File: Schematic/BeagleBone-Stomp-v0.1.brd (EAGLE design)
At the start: 100 x 80 mm, 8 parts, among them U1 MSP430G2553_RHB_32, U2 TLV320AIC3120_RHB_32

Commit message: connected a few of the pins in the design.
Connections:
- removed net AVDD: U2.17
- removed net SPKVDD: U2.24
- removed net SPKVSS: U2.25
- new net N$1: U$2.52, U2.24
- net 3.3V: now also U2.17
- net AVSS: no longer U2.16
- net GND: now also U2.16, U2.25
- net VDD_5V: no longer U$2.52
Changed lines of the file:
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@@
 <signal name="VDD_5V">
 <contactref element="U$2" pad="51"/>
-<contactref element="U$2" pad="52"/>
-<wire x1="69.85" y1="61.595" x2="69.85" y2="64.135" width="0" layer="19" extent="1-1"/>
-</signal>
-<signal name="VDD_ADC">
-<contactref element="U$2" pad="78"/>
-</signal>
-<signal name="GNDA_ADC">
-<contactref element="U$2" pad="80"/>
 </signal>
 <signal name="AGND">
@@
 <contactref element="U$2" pad="50"/>
 <contactref element="U$2" pad="49"/>
+<contactref element="U2" pad="17"/>
 <wire x1="72.39" y1="61.595" x2="72.39" y2="64.135" width="0" layer="19" extent="1-1"/>
+<wire x1="45.0088" y1="45.2374" x2="72.39" y2="61.595" width="0" layer="19" extent="1-1"/>
 </signal>
 <signal name="GND">
@@
 <contactref element="U$2" pad="90"/>
 <contactref element="U$2" pad="48"/>
-<wire x1="21.59" y1="64.135" x2="19.05" y2="64.135" width="0" layer="19" extent="1-1"/>
-<wire x1="19.05" y1="61.595" x2="19.05" y2="64.135" width="0" layer="19" extent="1-1"/>
-<wire x1="21.59" y1="61.595" x2="21.59" y2="64.135" width="0" layer="19" extent="1-1"/>
-<wire x1="74.93" y1="64.135" x2="21.59" y2="64.135" width="0" layer="19" extent="1-1"/>
+<contactref element="U2" pad="16"/>
+<contactref element="U2" pad="25"/>
 <wire x1="74.93" y1="61.595" x2="74.93" y2="64.135" width="0" layer="19" extent="1-1"/>
-<wire x1="74.93" y1="15.875" x2="74.93" y2="61.595" width="0" layer="19" extent="1-1"/>
+<wire x1="44.2976" y1="49.4538" x2="74.93" y2="61.595" width="0" layer="19" extent="1-1"/>
+<wire x1="44.2976" y1="44.5262" x2="44.2976" y2="49.4538" width="0" layer="19" extent="1-1"/>
+<wire x1="21.59" y1="61.595" x2="44.2976" y2="49.4538" width="0" layer="19" extent="1-1"/>
+<wire x1="21.59" y1="64.135" x2="21.59" y2="61.595" width="0" layer="19" extent="1-1"/>
+<wire x1="19.05" y1="64.135" x2="21.59" y2="64.135" width="0" layer="19" extent="1-1"/>
+<wire x1="19.05" y1="61.595" x2="21.59" y2="61.595" width="0" layer="19" extent="1-1"/>
+<wire x1="74.93" y1="15.875" x2="44.2976" y2="44.5262" width="0" layer="19" extent="1-1"/>
 <wire x1="74.93" y1="13.335" x2="74.93" y2="15.875" width="0" layer="19" extent="1-1"/>
 </signal>
@@
 <signal name="AVSS">
 <contactref element="U1" pad="27"/>
-<contactref element="U2" pad="16"/>
-<wire x1="43.307" y1="38.6588" x2="44.2976" y2="44.5262" width="0" layer="19" extent="1-1"/>
 </signal>
 <signal name="DVSS">
@@
 <contactref element="U2" pad="3"/>
 </signal>
-<signal name="AVDD">
-<contactref element="U2" pad="17"/>
-</signal>
 <signal name="SPKVSS_2">
 <contactref element="U2" pad="20"/>
@@
 <signal name="SPKVDD_2">
 <contactref element="U2" pad="21"/>
-</signal>
-<signal name="SPKVDD">
-<contactref element="U2" pad="24"/>
-</signal>
-<signal name="SPKVSS">
-<contactref element="U2" pad="25"/>
 </signal>
 <signal name="HPVDD">
@@
 <contactref element="U2" pad="29"/>
 </signal>
+<signal name="VDD_ADC">
+<contactref element="U$2" pad="78"/>
+</signal>
+<signal name="GNDA_ADC">
+<contactref element="U$2" pad="80"/>
+</signal>
+<signal name="N$1">
+<contactref element="U2" pad="24"/>
+<contactref element="U$2" pad="52"/>
+<wire x1="45.0088" y1="48.7426" x2="69.85" y2="61.595" width="0" layer="19" extent="1-1"/>
+</signal>
 </signals>

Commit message: Making some changes
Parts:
- added C1, C3, C4: 0.1u, microbuilder:0402
- added FB1: (no value), microbuilder:_0402
- added R1: 28k, microbuilder:0402
- added R2: 56.2k, microbuilder:0402
- added U3: TPS73701_DRB_8, bone:DRB8_1P75X1P5
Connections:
- removed net DVCC: U1.30
- removed net DVDD: U2.3
- removed net DVSS: U1.28, U2.18
- removed net IOVDD: U2.2
- removed net IOVSS: U2.1
- new net 1.8V: C4.2, R1.1, U2.3, U3.1
- net 3.3V: now also C1.1, U1.30, U2.2, U3.5, U3.8
- net 5.0V: now also C3.1, U2.24
- net AGND: now also FB1.1, U2.16, U2.33
- net GND: now also C1.2, C3.2, FB1.2, R2.1, U1.28, U2.1, U2.18, U3.4, U3.9; no longer U2.16
- net N$1: now also C4.1, R1.2, R2.2, U3.3; no longer U$2.52, U2.24
- net VDD_5V: now also U$2.52
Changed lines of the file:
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@@
 <attribute name="PACKAGE_DESIGNATOR" value="RHB" x="42.545" y="46.99" size="1.778" layer="27" display="off"/>
 </element>
+<element name="C1" library="microbuilder" package="0402" value="0.1u" x="1.905" y="-1.27"/>
+<element name="C3" library="microbuilder" package="0402" value="0.1u" x="1.905" y="-6.35"/>
+<element name="U3" library="bone" package="DRB8_1P75X1P5" value="TPS73701_DRB_8" x="4.445" y="-10.795">
+<attribute name="DATASHEETURL" value="http://www.ti.com/lit/gpn/TPS73701" x="4.445" y="-10.795" size="1.778" layer="27" display="off"/>
+<attribute name="PIN_COUNT" value="8" x="4.445" y="-10.795" size="1.778" layer="27" display="off"/>
+<attribute name="GENERIC_PART_NUMBER" value="TPS73701" x="4.445" y="-10.795" size="1.778" layer="27" display="off"/>
+<attribute name="DESCRIPTION" value="Single Output LDO, 1A, Adj. (1.2 to 5.0V), Reverse Current Protection" x="4.445" y="-10.795" size="1.778" layer="27" display="off"/>
+<attribute name="FAMILY_NAME" value="SINGLE CHANNEL LDO" x="4.445" y="-10.795" size="1.778" layer="27" display="off"/>
+<attribute name="MANUFACTURER" value="Texas Instruments" x="4.445" y="-10.795" size="1.778" layer="27" display="off"/>
+<attribute name="INDUSTRY_STD_PKG_TYPE" value="SON" x="4.445" y="-10.795" size="1.778" layer="27" display="off"/>
+<attribute name="VENDOR" value="Texas Instruments" x="4.445" y="-10.795" size="1.778" layer="27" display="off"/>
+<attribute name="MANUFACTURER_PART_NUMBER" value="tps73701_drb_8" x="4.445" y="-10.795" size="1.778" layer="27" display="off"/>
+<attribute name="PACKAGE_DESIGNATOR" value="DRB" x="4.445" y="-10.795" size="1.778" layer="27" display="off"/>
+</element>
+<element name="R1" library="microbuilder" package="0402" value="28k" x="1.905" y="-13.97"/>
+<element name="R2" library="microbuilder" package="0402" value="56.2k" x="1.905" y="-16.51"/>
+<element name="C4" library="microbuilder" package="0402" value="0.1u" x="1.905" y="-19.05"/>
+<element name="FB1" library="microbuilder" package="_0402" value="" x="1.905" y="-22.225"/>
 </elements>
 <signals>
 <signal name="VDD_5V">
 <contactref element="U$2" pad="51"/>
+<contactref element="U$2" pad="52"/>
+<wire x1="69.85" y1="61.595" x2="69.85" y2="64.135" width="0" layer="19" extent="1-1"/>
 </signal>
 <signal name="AGND">
 <contactref element="U$2" pad="38"/>
+<contactref element="U2" pad="16"/>
+<contactref element="U2" pad="33"/>
+<contactref element="FB1" pad="1"/>
+<wire x1="42.545" y1="46.99" x2="44.2976" y2="44.5262" width="0" layer="19" extent="1-1"/>
+<wire x1="29.21" y1="13.335" x2="44.2976" y2="44.5262" width="0" layer="19" extent="1-1"/>
+<wire x1="1.397" y1="-22.225" x2="29.21" y2="13.335" width="0" layer="19" extent="1-1"/>
 </signal>
 <signal name="5.0V">
 <contactref element="U$2" pad="53"/>
 <contactref element="U$2" pad="54"/>
+<contactref element="U2" pad="24"/>
+<contactref element="C3" pad="1"/>
 <wire x1="67.31" y1="61.595" x2="67.31" y2="64.135" width="0" layer="19" extent="1-1"/>
+<wire x1="45.0088" y1="48.7426" x2="67.31" y2="61.595" width="0" layer="19" extent="1-1"/>
+<wire x1="1.255" y1="-6.35" x2="45.0088" y2="48.7426" width="0" layer="19" extent="1-1"/>
 </signal>
 <signal name="3.3V">
@@
 <contactref element="U$2" pad="49"/>
 <contactref element="U2" pad="17"/>
+<contactref element="U1" pad="30"/>
+<contactref element="C1" pad="1"/>
+<contactref element="U2" pad="2"/>
+<contactref element="U3" pad="8"/>
+<contactref element="U3" pad="5"/>
 <wire x1="72.39" y1="61.595" x2="72.39" y2="64.135" width="0" layer="19" extent="1-1"/>
 <wire x1="45.0088" y1="45.2374" x2="72.39" y2="61.595" width="0" layer="19" extent="1-1"/>
+<wire x1="40.0812" y1="48.2346" x2="45.0088" y2="45.2374" width="0" layer="19" extent="1-1"/>
+<wire x1="41.783" y1="38.6588" x2="45.0088" y2="45.2374" width="0" layer="19" extent="1-1"/>
+<wire x1="1.255" y1="-1.27" x2="41.783" y2="38.6588" width="0" layer="19" extent="1-1"/>
+<wire x1="5.9182" y1="-9.8298" x2="1.255" y2="-1.27" width="0" layer="19" extent="1-1"/>
+<wire x1="5.9182" y1="-11.7602" x2="5.9182" y2="-9.8298" width="0" layer="19" extent="1-1"/>
 </signal>
 <signal name="GND">
@@
 <contactref element="U$2" pad="90"/>
 <contactref element="U$2" pad="48"/>
-<contactref element="U2" pad="16"/>
+<contactref element="U1" pad="28"/>
 <contactref element="U2" pad="25"/>
+<contactref element="U2" pad="1"/>
+<contactref element="C3" pad="2"/>
+<contactref element="C1" pad="2"/>
+<contactref element="U3" pad="4"/>
+<contactref element="U3" pad="9"/>
+<contactref element="U3" pad="4"/>
+<contactref element="R2" pad="1"/>
+<contactref element="U2" pad="18"/>
+<contactref element="FB1" pad="2"/>
 <wire x1="74.93" y1="61.595" x2="74.93" y2="64.135" width="0" layer="19" extent="1-1"/>
 <wire x1="44.2976" y1="49.4538" x2="74.93" y2="61.595" width="0" layer="19" extent="1-1"/>
-<wire x1="44.2976" y1="44.5262" x2="44.2976" y2="49.4538" width="0" layer="19" extent="1-1"/>
-<wire x1="21.59" y1="61.595" x2="44.2976" y2="49.4538" width="0" layer="19" extent="1-1"/>
+<wire x1="45.0088" y1="45.7454" x2="44.2976" y2="49.4538" width="0" layer="19" extent="1-1"/>
+<wire x1="40.0812" y1="48.7426" x2="44.2976" y2="49.4538" width="0" layer="19" extent="1-1"/>
+<wire x1="42.799" y1="38.6588" x2="45.0088" y2="45.7454" width="0" layer="19" extent="1-1"/>
+<wire x1="21.59" y1="61.595" x2="40.0812" y2="48.7426" width="0" layer="19" extent="1-1"/>
 <wire x1="21.59" y1="64.135" x2="21.59" y2="61.595" width="0" layer="19" extent="1-1"/>
 <wire x1="19.05" y1="64.135" x2="21.59" y2="64.135" width="0" layer="19" extent="1-1"/>
 <wire x1="19.05" y1="61.595" x2="21.59" y2="61.595" width="0" layer="19" extent="1-1"/>
-<wire x1="74.93" y1="15.875" x2="44.2976" y2="44.5262" width="0" layer="19" extent="1-1"/>
+<wire x1="74.93" y1="15.875" x2="42.799" y2="38.6588" width="0" layer="19" extent="1-1"/>
 <wire x1="74.93" y1="13.335" x2="74.93" y2="15.875" width="0" layer="19" extent="1-1"/>
+<wire x1="2.555" y1="-1.27" x2="42.799" y2="38.6588" width="0" layer="19" extent="1-1"/>
+<wire x1="2.555" y1="-6.35" x2="2.555" y2="-1.27" width="0" layer="19" extent="1-1"/>
+<wire x1="4.445" y1="-10.795" x2="2.555" y2="-6.35" width="0" layer="19" extent="1-1"/>
+<wire x1="2.9718" y1="-11.7602" x2="4.445" y2="-10.795" width="0" layer="19" extent="1-1"/>
+<wire x1="1.255" y1="-16.51" x2="2.9718" y2="-11.7602" width="0" layer="19" extent="1-1"/>
+<wire x1="2.413" y1="-22.225" x2="1.255" y2="-16.51" width="0" layer="19" extent="1-1"/>
 </signal>
 <signal name="AVCC">
@@
 <signal name="AVSS">
 <contactref element="U1" pad="27"/>
-</signal>
-<signal name="DVSS">
-<contactref element="U1" pad="28"/>
-<contactref element="U2" pad="18"/>
-<wire x1="42.799" y1="38.6588" x2="45.0088" y2="45.7454" width="0" layer="19" extent="1-1"/>
-</signal>
-<signal name="DVCC">
-<contactref element="U1" pad="30"/>
-</signal>
-<signal name="IOVSS">
-<contactref element="U2" pad="1"/>
-</signal>
-<signal name="IOVDD">
-<contactref element="U2" pad="2"/>
-</signal>
-<signal name="DVDD">
-<contactref element="U2" pad="3"/>
 </signal>
 <signal name="SPKVSS_2">
@@
 <contactref element="U$2" pad="80"/>
 </signal>
+<signal name="1.8V">
+<contactref element="U2" pad="3"/>
+<contactref element="U3" pad="1"/>
+<contactref element="R1" pad="1"/>
+<contactref element="C4" pad="2"/>
+<wire x1="2.9718" y1="-9.8298" x2="40.0812" y2="47.752" width="0" layer="19" extent="1-1"/>
+<wire x1="1.255" y1="-13.97" x2="2.9718" y2="-9.8298" width="0" layer="19" extent="1-1"/>
+<wire x1="2.555" y1="-19.05" x2="1.255" y2="-13.97" width="0" layer="19" extent="1-1"/>
+</signal>
 <signal name="N$1">
-<contactref element="U2" pad="24"/>
-<contactref element="U$2" pad="52"/>
-<wire x1="45.0088" y1="48.7426" x2="69.85" y2="61.595" width="0" layer="19" extent="1-1"/>
+<contactref element="C4" pad="1"/>
+<contactref element="R1" pad="2"/>
+<contactref element="R2" pad="2"/>
+<contactref element="U3" pad="3"/>
+<wire x1="2.555" y1="-16.51" x2="1.255" y2="-19.05" width="0" layer="19" extent="1-1"/>
+<wire x1="2.555" y1="-13.97" x2="2.555" y2="-16.51" width="0" layer="19" extent="1-1"/>
+<wire x1="2.9718" y1="-11.1252" x2="2.555" y2="-13.97" width="0" layer="19" extent="1-1"/>
 </signal>
 </signals>

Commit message: Adding MSP430 connections
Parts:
- added C10, C11, C12, C2, C7, C9: 10u, microbuilder:0805
- added C13, C14, C5, C6, C8: 0.1u, microbuilder:0402
- added GND, RST, SPKM, SPKP, TST, VCC: WIREPAD2,15/1,0, wirepad:2,15/1,0
- added R10, R11, R12, R13, R14, R15, R16: 10k, microbuilder:0402
- added R3, R4, R5, R6, R7, R8, R9: 470, microbuilder:0402
- moved U3 75.9 mm to (40.6, 55.9)
- turned U1 to 90 degrees
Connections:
- removed net AVSS: U1.27
- removed net HPVDD: U2.28
- removed net HPVSS: U2.29
- new net N$10: C11.1, U2.14
- new net N$11: C12.1, U2.13
- new net N$12: JP2.6, U1.31
- new net N$13: JP2.14, R9.2
- new net N$14: JP2.15, R8.2
- new net N$15: JP2.16, R7.2
- new net N$16: JP2.17, R6.2
- new net N$17: JP2.1, U1.5
- new net N$18: JP2.2, U1.4
- new net N$19: JP2.4, U1.2
- new net N$20: JP2.5, U1.1
- new net N$21: JP2.3, U1.3
- new net N$22: JP2.18, R5.2
- new net N$23: JP2.19, R4.2
- new net N$24: JP2.20, R3.2
- new net N$25: JP1.19, U1.15
- new net N$26: JP1.20, U1.14
- new net N$27: JP1.14, U1.20
- new net N$28: JP1.15, U1.19
- new net N$29: JP1.16, U1.18
- new net N$3: SPKM.1, U2.23
- new net N$30: JP1.17, U1.17
- new net N$31: JP1.18, U1.16
- new net N$32: TST.1, U1.24
- new net N$33: RST.1, U1.23
- new net N$34: JP2.7, R16.2, U1.6
- new net N$35: JP2.8, R15.2, U1.7
- new net N$36: JP2.9, R14.2, U1.9
- new net N$37: JP2.10, R13.2, U1.10
- new net N$38: JP2.11, R12.2, U1.11
- new net N$39: JP2.12, R11.2, U1.12
- new net N$4: SPKP.1, U2.26
- new net N$40: JP2.13, R10.2, U1.13
- new net N$5: C10.1, U2.27
- new net N$6: C10.2, U$7.T
- new net N$7: C9.2, U$7.S
- new net N$8: C12.2, U$1.S
- new net N$9: C11.2, U$1.T
- net 1.8V: now also C5.1
- net 3.3V: now also C13.1, C14.1, C2.1, C6.1, C7.1, C8.1, JP3.1, JP3.2, JP3.3, JP3.4, JP3.5, JP3.6, R10.1, R11.1, R12.1, R13.1, R14.1, R15.1, R16.1, R3.1, R4.1, R5.1, R6.1, R7.1, R8.1, R9.1, U1.29, U2.28, VCC.1
- net AGND: now also C13.2, C2.2, C6.2, U1.27, U1.33
- net AVCC: no longer U1.29
- net GND: now also C14.2, C5.2, C7.2, C8.2, C9.1, GND.1, JP1.1, JP1.10, JP1.11, JP1.12, JP1.13, JP1.2, JP1.3, JP1.4, JP1.5, JP1.6, JP1.7, JP1.8, JP1.9, U2.29

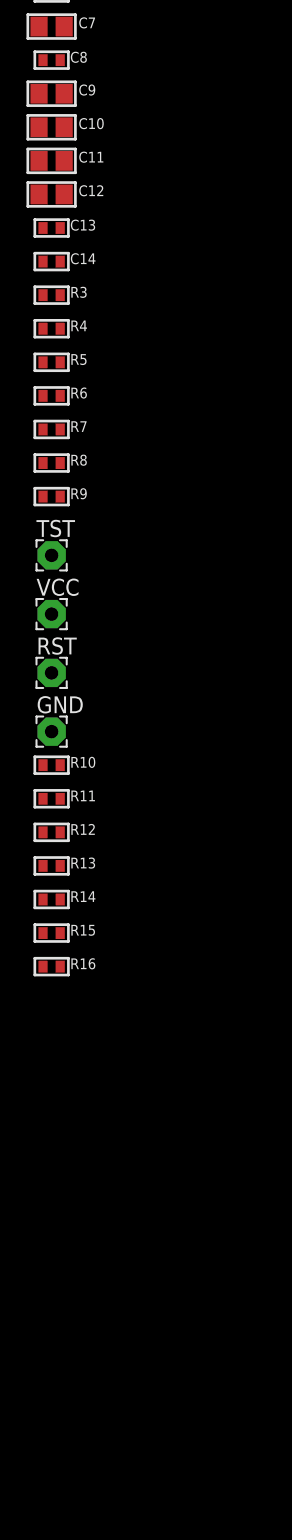
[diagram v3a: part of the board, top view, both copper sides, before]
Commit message: Adding crystal and a couple caps. Also added codec connections
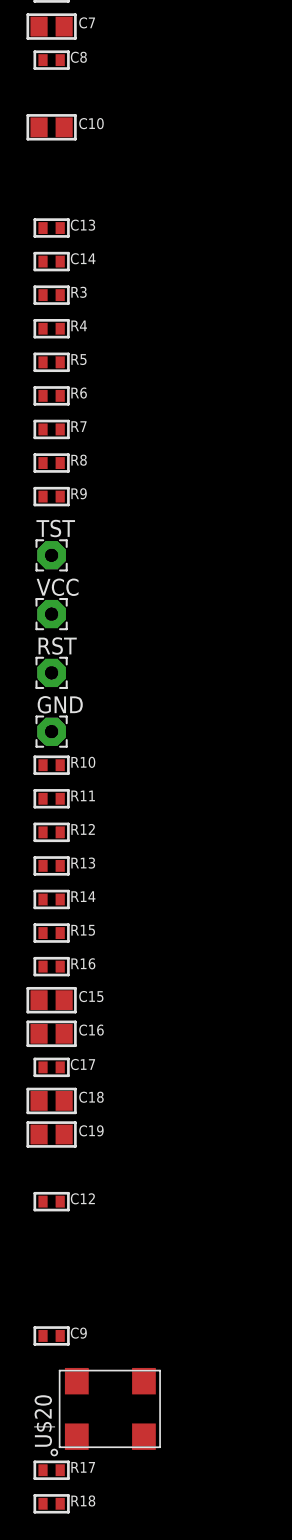
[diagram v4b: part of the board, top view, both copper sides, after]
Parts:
- removed C11: 10u, microbuilder:0805
- added C15, C16: 22u, microbuilder:0805
- added C17: 0.1u, microbuilder:0402
- added C18, C19: 10u, microbuilder:0805
- added R17, R18: 4.7k, microbuilder:0402
- added U$20: FXO-HC735-12, bone:FXO-HC735-12
- C10: value 10u -> 47u
- C12: value 10u -> 0.1u; device microbuilder:0805 -> microbuilder:0402
- C9: value 10u -> 0.01u; device microbuilder:0805 -> microbuilder:0402
- moved C9 94.0 mm to (1.91, -128.9)
- moved C12 76.2 mm to (1.91, -118.7)
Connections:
- removed net N$7 (its old number): C9.2, U$7.S
- removed net SPKVDD_2: U2.21
- removed net SPKVSS_2: U2.20
- new net N$24: U$2.71, U2.5
- new net N$41: U$2.75, U2.6
- new net N$42: U$2.77, U2.7
- new net N$43: C16.1, C17.1, U2.21
- new net N$44: R18.1, U$2.66, U1.22, U2.9
- new net N$45: U$2.56, U2.31
- new net N$46: R17.1, U$2.65, U1.21, U2.10
- net 1.8V: now also C18.1
- net 3.3V: now also C19.1, C9.1, R17.2, R18.2, U$20.VDD
- net 5.0V: now also C15.1
- net AGND: now also C15.2, C16.2, C17.2, C3.2, C7.2, C8.2, U$1.S, U$7.S, U2.20, U2.25, U2.29
- net GND: now also C18.2, C19.2, C9.2, U$20.GND; no longer C3.2, C7.2, C8.2, C9.1, U2.25, U2.29
- net N$10: now also C12.2; no longer C11.1
- net N$11: now also U$2.74, U2.4; no longer C12.1, U2.13
- net N$3: now also U2.19
- net N$4: now also U2.22
- net N$8: now also U$20.OUT, U2.8; no longer C12.2, U$1.S
- net N$9: now also C12.1; no longer C11.2
